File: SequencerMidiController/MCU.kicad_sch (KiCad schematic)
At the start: 7 parts, among them U33 STM32G0B1_KxTxN_LQFP32

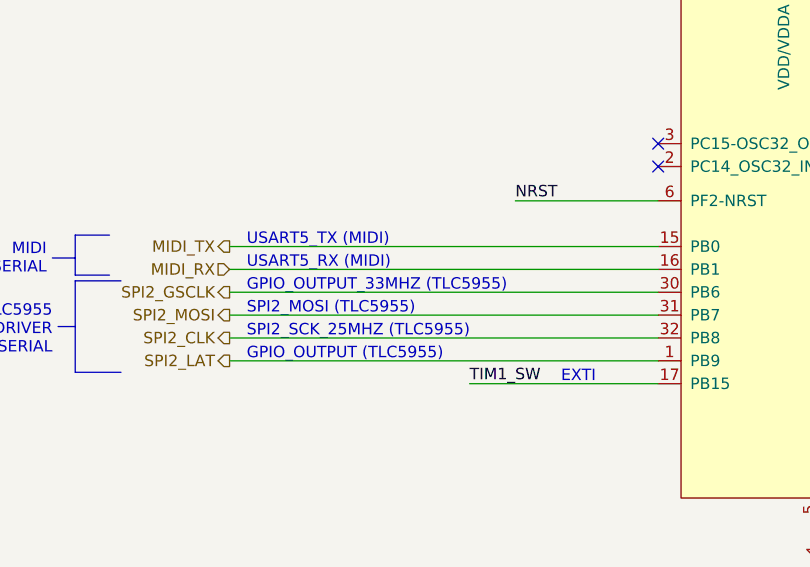
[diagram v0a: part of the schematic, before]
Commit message: updated SPI labels
https://github.com/cracked-machine/BassStationSequencerMidiController/issues/3
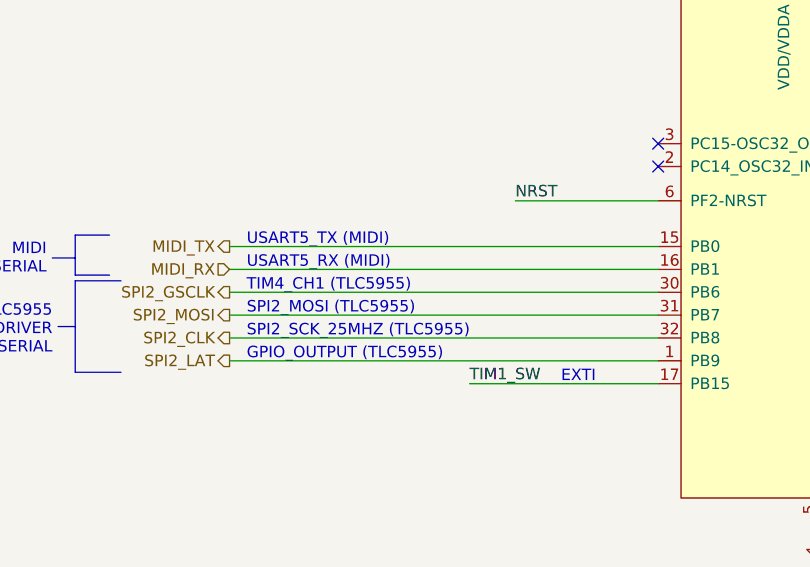
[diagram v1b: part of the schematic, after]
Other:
- note added: "TIM4_CH1 (TLC5955)"
- note removed: "GPIO_OUTPUT_33MHZ (TLC5955)"
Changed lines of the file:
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@@
     (effects (font (size 1.27 1.27)) (justify left bottom))
   )
-  (text "GPIO_OUTPUT_33MHZ (TLC5955)" (at 202.565 117.475 0)
+  (text "TIM4_CH1 (TLC5955)" (at 202.565 117.475 0)
     (effects (font (size 1.27 1.27)) (justify left bottom))
   )
